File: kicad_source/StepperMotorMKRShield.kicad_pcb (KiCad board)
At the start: 2 copper layers, 100 x 60 mm, 112 parts, among them CN1 ARDUINO_MKR, CN10 691322310004, CN11 BM05B-SRSS-TB, CN2 DNI, CN20 691322310004, CN21 BM05B-SRSS-TB, CN3 BM04B-SRSS-TB, CN4 CONN_01X04, CN5 691322310002, CN6 691313710002, CN7 ARDUINO_NANO_33, Q1 IPD90P03P4L- 04, U1 TMC5130A-TA, U2 TMC5130A-TA, U4 LM75BD, U9 IFX91041EJV, Y1 ECS-3225MV-160-BN-TR

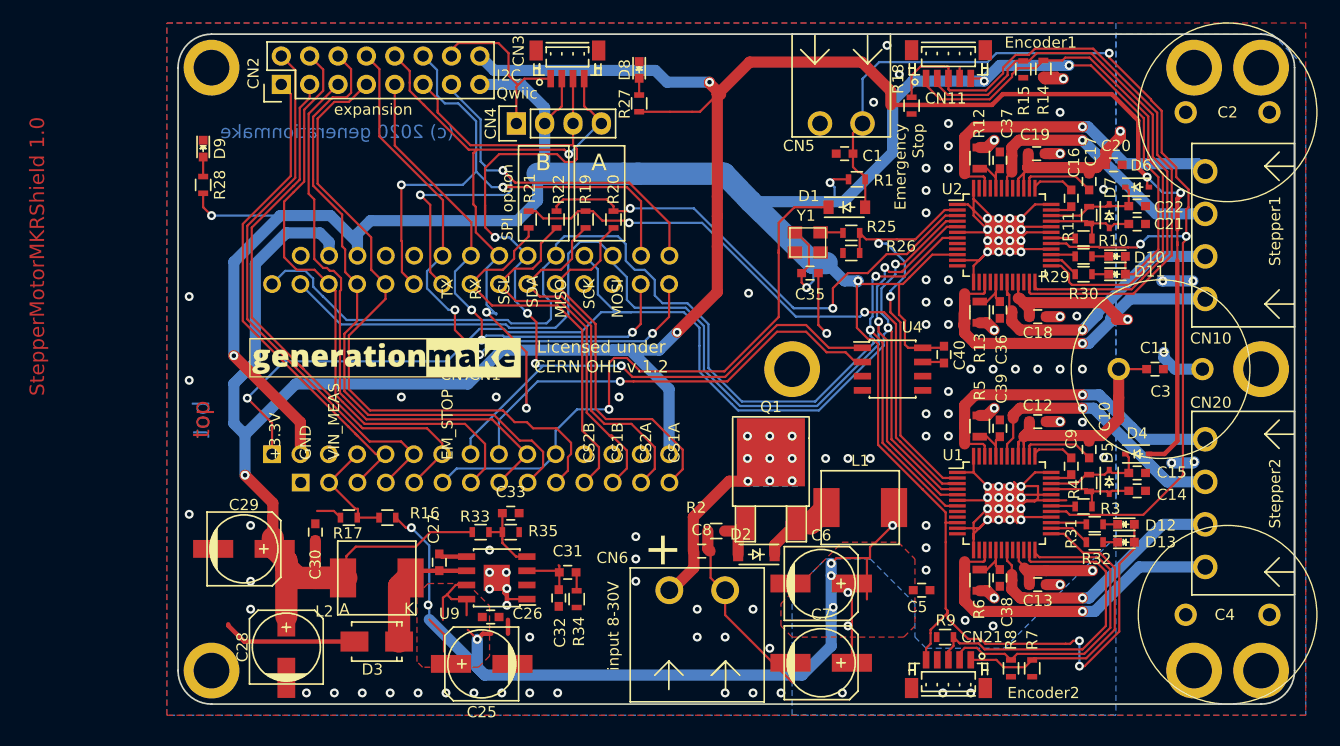
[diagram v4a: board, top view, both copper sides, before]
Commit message: updated layout
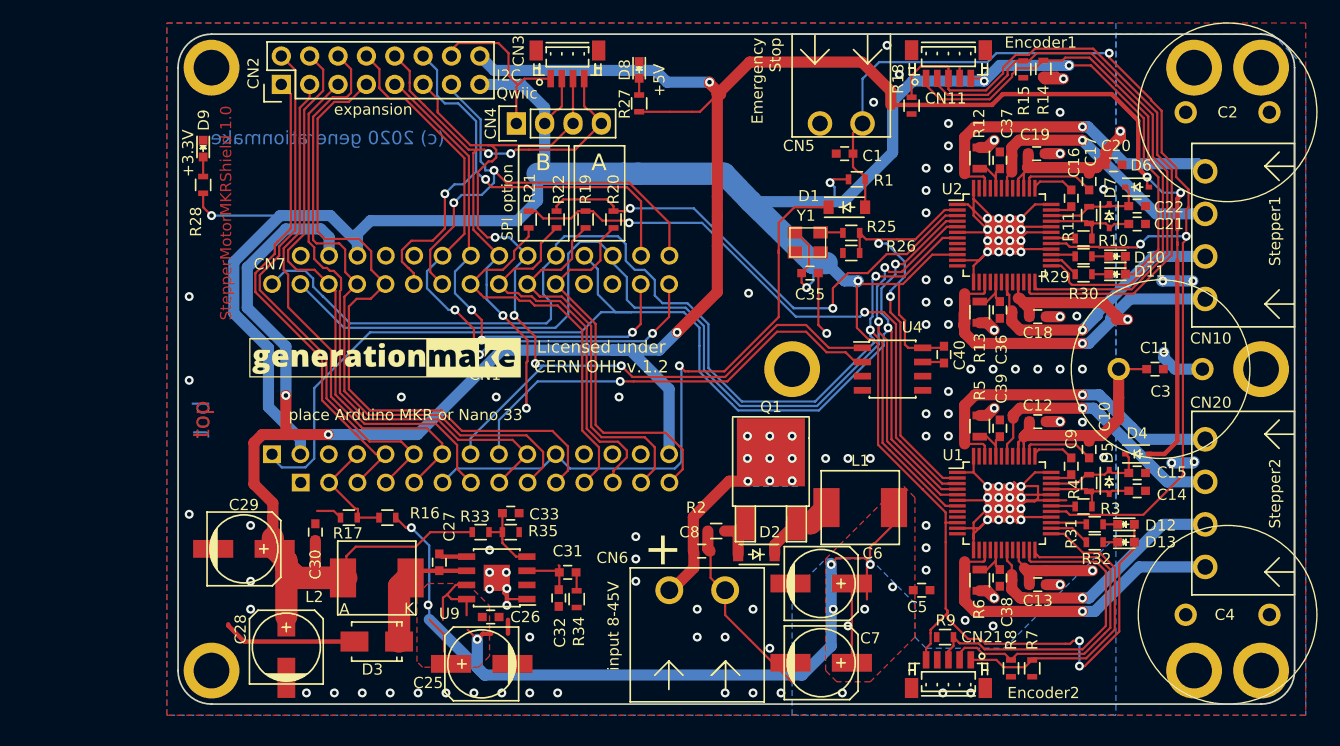
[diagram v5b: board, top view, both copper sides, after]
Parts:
- CN1: footprint MODULE_compute:ARDUINO_MKR -> MODULE_compute:ARDUINO_MKR_BASEBOARD
- moved L4 36.9 mm to (70.1, 80.9)
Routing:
- net I2C_SDA: track 97.9 -> 89.6 mm
- net /D6: track 49.5 -> 44.4 mm
- net /A5: track 54.3 -> 51.5 mm
- net /A3: track 50.0 -> 47.2 mm
- net /SER_TX: track 53.8 -> 56.2 mm
- net EM_STOP_D: track 54.7 -> 56.8 mm
- net /D1: track 59.8 -> 61.7 mm
- net /D7: track 50.3 -> 48.7 mm
- net I2C_SCL: track 98.4 -> 96.9 mm, vias 4 -> 5
- net SCK: track 115.6 -> 114.1 mm, vias 3 -> 2
- net /D0: track 58.1 -> 59.3 mm
- net /A2: track 49.4 -> 48.4 mm
- net /A1: track 44.9 -> 44.0 mm
- net /CS1A: track 33.7 -> 34.6 mm
- net /CS2A: track 33.8 -> 34.7 mm
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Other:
- board text added: "+5V"
- board text added: "input 8-45V"
- board text added: "place Arduino MKR or Nano 33"
- board text removed: "CS1A"
- board text removed: "CS1B"
- board text removed: "CS2A"
- board text removed: "CS2B"
- board text removed: "EM_STOP"
- board text removed: "GND"
- board text removed: "MISO"
- board text removed: "MOSI"
- board text removed: "RX"
- board text removed: "SCK"
- board text removed: "SCL"
- board text removed: "SDA"
- board text removed: "TX"
- board text removed: "VIN_MEAS"
- board text removed: "input 8-30V"
